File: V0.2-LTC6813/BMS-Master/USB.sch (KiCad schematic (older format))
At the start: 11 parts

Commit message: Schematics 90% completed
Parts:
- gave numbers to parts that had none: 11
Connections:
- no-connect marks 0 -> 13
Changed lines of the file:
@@
 $EndDescr
 $Comp
-L Interface_USB:CP2104 U?
+L Interface_USB:CP2104 U7
 U 1 1 5C246DA5
 P 5350 3600
-F 0 "U?" H 5350 2511 50  0000 C CNN
-F 1 "CP2104" H 5350 2420 50  0000 C CNN
+F 0 "U7" H 5900 4700 50  0000 C CNN
+F 1 "CP2104" H 5800 4600 50  0000 C CNN
 F 2 "Package_DFN_QFN:QFN-24-1EP_4x4mm_P0.5mm_EP2.6x2.6mm" H 5500 2650 50  0001 L CNN
 F 3 "https://www.silabs.com/Support%20Documents/TechnicalDocs/cp2104.pdf" H 4800 4850 50  0001 C CNN
@@
 $EndComp
 $Comp
-L power:GND #PWR?
+L power:GND #PWR0172
 U 1 1 5C2E18AB
 P 5300 5000
-F 0 "#PWR?" H 5300 4750 50  0001 C CNN
+F 0 "#PWR0172" H 5300 4750 50  0001 C CNN
 F 1 "GND" H 5305 4827 50  0000 C CNN
 F 2 "" H 5300 5000 50  0001 C CNN
@@
 Connection ~ 5300 5000
 $Comp
-L Device:R R?
+L Device:R R111
 U 1 1 5C2E2764
 P 3900 3500
-F 0 "R?" V 3850 3700 50  0000 C CNN
+F 0 "R111" V 3850 3700 50  0000 C CNN
 F 1 "240" V 3850 3300 50  0000 C CNN
 F 2 "Resistors_SMD:R_0603_HandSoldering" V 3830 3500 50  0001 C CNN
@@
 $EndComp
 $Comp
-L Device:R R?
+L Device:R R112
 U 1 1 5C2E33F0
 P 3900 3600
-F 0 "R?" V 3850 3800 50  0000 C CNN
+F 0 "R112" V 3850 3800 50  0000 C CNN
 F 1 "240" V 3850 3400 50  0000 C CNN
 F 2 "Resistors_SMD:R_0603_HandSoldering" V 3830 3600 50  0001 C CNN
@@
 Vusb
 $Comp
-L Power_Protection:SP0502BAHT D?
+L Power_Protection:SP0502BAHT D3
 U 1 1 5C2FBFBC
 P 6800 4150
-F 0 "D?" H 7005 4196 50  0000 L CNN
+F 0 "D3" H 7005 4196 50  0000 L CNN
 F 1 "SP0502BAHT" H 7005 4105 50  0000 L CNN
 F 2 "Package_TO_SOT_SMD:SOT-23" H 7025 4100 50  0001 L CNN
@@
 $EndComp
 $Comp
-L power:GND #PWR?
+L power:GND #PWR0173
 U 1 1 5C2FC79C
 P 6800 4450
-F 0 "#PWR?" H 6800 4200 50  0001 C CNN
+F 0 "#PWR0173" H 6800 4200 50  0001 C CNN
 F 1 "GND" H 6805 4277 50  0000 C CNN
 F 2 "" H 6800 4450 50  0001 C CNN
@@
 	6900 3600 6900 3950
 $Comp
-L Device:R R?
+L Device:R R113
 U 1 1 5C2FD55A
 P 4050 4100
-F 0 "R?" V 4000 4300 50  0000 C CNN
+F 0 "R113" V 4000 4300 50  0000 C CNN
 F 1 "10k" V 4000 3900 50  0000 C CNN
 F 2 "Resistors_SMD:R_0603_HandSoldering" V 3980 4100 50  0001 C CNN
@@
 	4200 4100 4650 4100
 $Comp
-L Device:C C?
+L Device:C C40
 U 1 1 5C2FE444
 P 6150 4600
-F 0 "C?" H 6265 4646 50  0000 L CNN
+F 0 "C40" H 6265 4646 50  0000 L CNN
 F 1 "2.2u" H 6265 4555 50  0000 L CNN
 F 2 "Capacitors_SMD:C_0603_HandSoldering" H 6188 4450 50  0001 C CNN
@@
 	6150 4300 6050 4300
 $Comp
-L power:GND #PWR?
+L power:GND #PWR0174
 U 1 1 5C2FEB38
 P 6150 4950
-F 0 "#PWR?" H 6150 4700 50  0001 C CNN
+F 0 "#PWR0174" H 6150 4700 50  0001 C CNN
 F 1 "GND" H 6155 4777 50  0000 C CNN
 F 2 "" H 6150 4950 50  0001 C CNN
@@
 	6150 4750 6150 4950
 $Comp
-L Device:C C?
+L Device:C C39
 U 1 1 5C2FEEC7
 P 4300 2050
-F 0 "C?" H 4415 2096 50  0000 L CNN
+F 0 "C39" H 4415 2096 50  0000 L CNN
 F 1 "2.2u" H 4415 2005 50  0000 L CNN
 F 2 "Capacitors_SMD:C_0603_HandSoldering" H 4338 1900 50  0001 C CNN
@@
 $EndComp
 $Comp
-L power:GND #PWR?
+L power:GND #PWR0175
 U 1 1 5C2FF845
 P 4300 2300
-F 0 "#PWR?" H 4300 2050 50  0001 C CNN
+F 0 "#PWR0175" H 4300 2050 50  0001 C CNN
 F 1 "GND" H 4305 2127 50  0000 C CNN
 F 2 "" H 4300 2300 50  0001 C CNN
@@
 Connection ~ 5350 1900
 $Comp
-L power:VDD #PWR?
+L power:VDD #PWR0176
 U 1 1 5C300C10
 P 7350 1700
-F 0 "#PWR?" H 7350 1550 50  0001 C CNN
+F 0 "#PWR0176" H 7350 1550 50  0001 C CNN
 F 1 "VDD" H 7367 1873 50  0000 C CNN
 F 2 "" H 7350 1700 50  0001 C CNN
@@
 	7350 1750 7350 1700
 $Comp
-L power:VDD #PWR?
+L power:VDD #PWR0177
 U 1 1 5C3014B2
 P 5000 1900
-F 0 "#PWR?" H 5000 1750 50  0001 C CNN
+F 0 "#PWR0177" H 5000 1750 50  0001 C CNN
 F 1 "VDD" H 5017 2073 50  0000 C CNN
 F 2 "" H 5000 1900 50  0001 C CNN
@@
 	5000 1900 4300 1900
 $Comp
-L power:VDD #PWR?
+L power:VDD #PWR0178
 U 1 1 5C30198E
 P 3450 4100
-F 0 "#PWR?" H 3450 3950 50  0001 C CNN
+F 0 "#PWR0178" H 3450 3950 50  0001 C CNN
 F 1 "VDD" H 3467 4273 50  0000 C CNN
 F 2 "" H 3450 4100 50  0001 C CNN
@@
 	3450 4100 3900 4100
 $Comp
-L Device:C C?
+L Device:C C42
 U 1 1 5C302395
 P 6800 1900
-F 0 "C?" H 6915 1946 50  0000 L CNN
+F 0 "C42" H 6915 1946 50  0000 L CNN
 F 1 "2.2u" H 6915 1855 50  0000 L CNN
 F 2 "Capacitors_SMD:C_0603_HandSoldering" H 6838 1750 50  0001 C CNN
@@
 $EndComp
 $Comp
-L Device:C C?
+L Device:C C41
 U 1 1 5C3026E1
 P 6400 1900
-F 0 "C?" H 6515 1946 50  0000 L CNN
+F 0 "C41" H 6515 1946 50  0000 L CNN
 F 1 "100n" H 6515 1855 50  0000 L CNN
 F 2 "Capacitors_SMD:C_0603_HandSoldering" H 6438 1750 50  0001 C CNN
@@
 Connection ~ 7350 1750
 $Comp
-L Device:R R?
+L Device:R R114
 U 1 1 5C304BD5
 P 7350 1900
-F 0 "R?" H 7450 1950 50  0000 C CNN
+F 0 "R114" H 7450 1950 50  0000 C CNN
 F 1 "10k" H 7500 1850 50  0000 C CNN
 F 2 "Resistors_SMD:R_0603_HandSoldering" V 7280 1900 50  0001 C CNN
@@
 $EndComp
 $Comp
-L power:GND #PWR?
+L power:GND #PWR0179
 U 1 1 5C305761
 P 6400 2200
-F 0 "#PWR?" H 6400 1950 50  0001 C CNN
+F 0 "#PWR0179" H 6400 1950 50  0001 C CNN
 F 1 "GND" H 6405 2027 50  0000 C CNN
 F 2 "" H 6400 2200 50  0001 C CNN
@@
 $EndComp
 $Comp
-L power:GND #PWR?
+L power:GND #PWR0180
 U 1 1 5C30598A
 P 6800 2200
-F 0 "#PWR?" H 6800 1950 50  0001 C CNN
+F 0 "#PWR0180" H 6800 1950 50  0001 C CNN
 F 1 "GND" H 6805 2027 50  0000 C CNN
 F 2 "" H 6800 2200 50  0001 C CNN
@@
 $EndComp
 $Comp
-L power:GND #PWR?
+L power:GND #PWR0181
 U 1 1 5C305C03
 P 7350 2200
-F 0 "#PWR?" H 7350 1950 50  0001 C CNN
+F 0 "#PWR0181" H 7350 1950 50  0001 C CNN
 F 1 "GND" H 7355 2027 50  0000 C CNN
 F 2 "" H 7350 2200 50  0001 C CNN
@@
 	6400 2050 6400 2200
 $Comp
-L Transistor_FET:BSS138 Q?
+L Transistor_FET:BSS138 Q26
 U 1 1 5C307737
 P 8650 1750
-F 0 "Q?" H 8856 1796 50  0000 L CNN
+F 0 "Q26" H 8856 1796 50  0000 L CNN
 F 1 "BSS138" H 8856 1705 50  0000 L CNN
 F 2 "Package_TO_SOT_SMD:SOT-23" H 8850 1675 50  0001 L CIN
@@
 Connection ~ 7900 1750
 $Comp
-L power:GND #PWR?
+L power:GND #PWR0182
 U 1 1 5C30B1D5
 P 8750 2250
-F 0 "#PWR?" H 8750 2000 50  0001 C CNN
+F 0 "#PWR0182" H 8750 2000 50  0001 C CNN
 F 1 "GND" H 8755 2077 50  0000 C CNN
 F 2 "" H 8750 2250 50  0001 C CNN
@@
 Wire Wire Line
 	9300 1550 9300 1400
+NoConn ~ 5150 2700
+NoConn ~ 4650 3000
+NoConn ~ 4650 3100
+NoConn ~ 4650 3200
+NoConn ~ 4650 3300
+NoConn ~ 4650 3800
+NoConn ~ 4650 3900
+NoConn ~ 4650 4200
+NoConn ~ 4650 4300
+NoConn ~ 6050 3800
+NoConn ~ 6050 3900
+NoConn ~ 6050 4000
+NoConn ~ 6050 4100
 $EndSCHEMATC

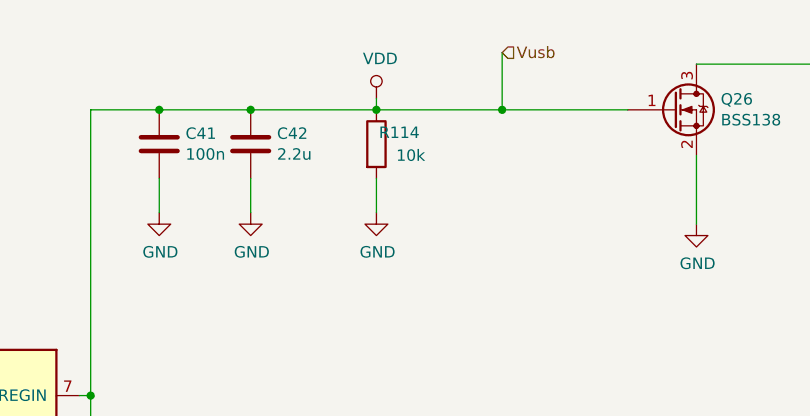
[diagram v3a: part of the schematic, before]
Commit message: Schematics 95% completed
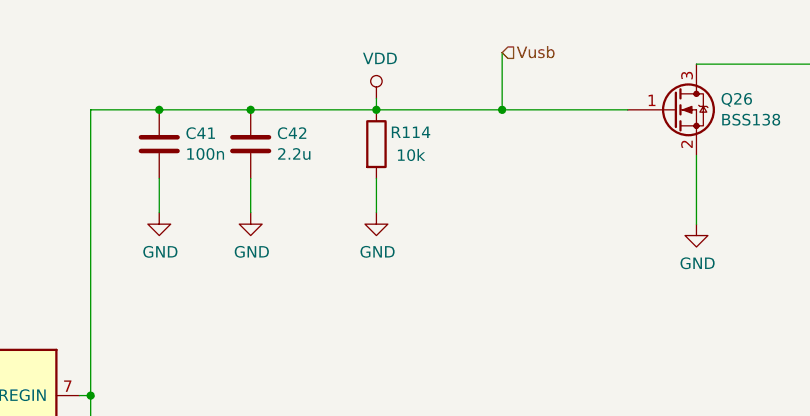
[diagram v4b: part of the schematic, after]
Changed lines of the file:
@@
 U 1 1 5C304BD5
 P 7350 1900
-F 0 "R114" H 7450 1950 50  0000 C CNN
+F 0 "R114" H 7500 1950 50  0000 C CNN
 F 1 "10k" H 7500 1850 50  0000 C CNN
 F 2 "Resistors_SMD:R_0603_HandSoldering" V 7280 1900 50  0001 C CNN

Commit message: PCB started
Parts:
- D3, Q26: footprint Package_TO_SOT_SMD:SOT-23 -> TO_SOT_Packages_SMD:SOT-23
- U7: footprint Package_DFN_QFN:QFN-24-1EP_4x4mm_P0.5mm_EP2.6x2.6mm -> Housings_DFN_QFN:QFN-24-1EP_4x4mm_Pitch0.5mm
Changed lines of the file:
@@
 F 0 "U7" H 5900 4700 50  0000 C CNN
 F 1 "CP2104" H 5800 4600 50  0000 C CNN
-F 2 "Package_DFN_QFN:QFN-24-1EP_4x4mm_P0.5mm_EP2.6x2.6mm" H 5500 2650 50  0001 L CNN
+F 2 "Housings_DFN_QFN:QFN-24-1EP_4x4mm_Pitch0.5mm" H 5500 2650 50  0001 L CNN
 F 3 "https://www.silabs.com/Support%20Documents/TechnicalDocs/cp2104.pdf" H 4800 4850 50  0001 C CNN
 	1    5350 3600
@@
 F 0 "D3" H 7005 4196 50  0000 L CNN
 F 1 "SP0502BAHT" H 7005 4105 50  0000 L CNN
-F 2 "Package_TO_SOT_SMD:SOT-23" H 7025 4100 50  0001 L CNN
+F 2 "TO_SOT_Packages_SMD:SOT-23" H 7025 4100 50  0001 L CNN
 F 3 "http://www.littelfuse.com/~/media/files/littelfuse/technical%20resources/documents/data%20sheets/sp05xxba.pdf" H 6925 4275 50  0001 C CNN
 	1    6800 4150
@@
 Wire Wire Line
 	6400 2050 6400 2200
-$Comp
-L Transistor_FET:BSS138 Q26
-U 1 1 5C307737
-P 8650 1750
-F 0 "Q26" H 8856 1796 50  0000 L CNN
-F 1 "BSS138" H 8856 1705 50  0000 L CNN
-F 2 "Package_TO_SOT_SMD:SOT-23" H 8850 1675 50  0001 L CIN
-F 3 "https://www.fairchildsemi.com/datasheets/BS/BSS138.pdf" H 8650 1750 50  0001 L CNN
-	1    8650 1750
-	1    0    0    -1
-$EndComp
 Wire Wire Line
 	7900 1500 7900 1750
@@
 NoConn ~ 6050 4000
 NoConn ~ 6050 4100
+$Comp
+L Transistor_FET:BSS138 Q26
+U 1 1 5C307737
+P 8650 1750
+F 0 "Q26" H 8856 1796 50  0000 L CNN
+F 1 "BSS138" H 8856 1705 50  0000 L CNN
+F 2 "TO_SOT_Packages_SMD:SOT-23" H 8850 1675 50  0001 L CIN
+F 3 "https://www.fairchildsemi.com/datasheets/BS/BSS138.pdf" H 8650 1750 50  0001 L CNN
+	1    8650 1750
+	1    0    0    -1
+$EndComp
 $EndSCHEMATC
